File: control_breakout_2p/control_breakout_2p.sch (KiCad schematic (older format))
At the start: 8 parts, among them J1 DB15_Female_MountingHoles, J2 DB15_Female_MountingHoles, J3 Conn_02x12_Row_Letter_Last, J4 Conn_02x12_Row_Letter_Last, J5 Screw_Terminal_01x06, J6 Screw_Terminal_01x06

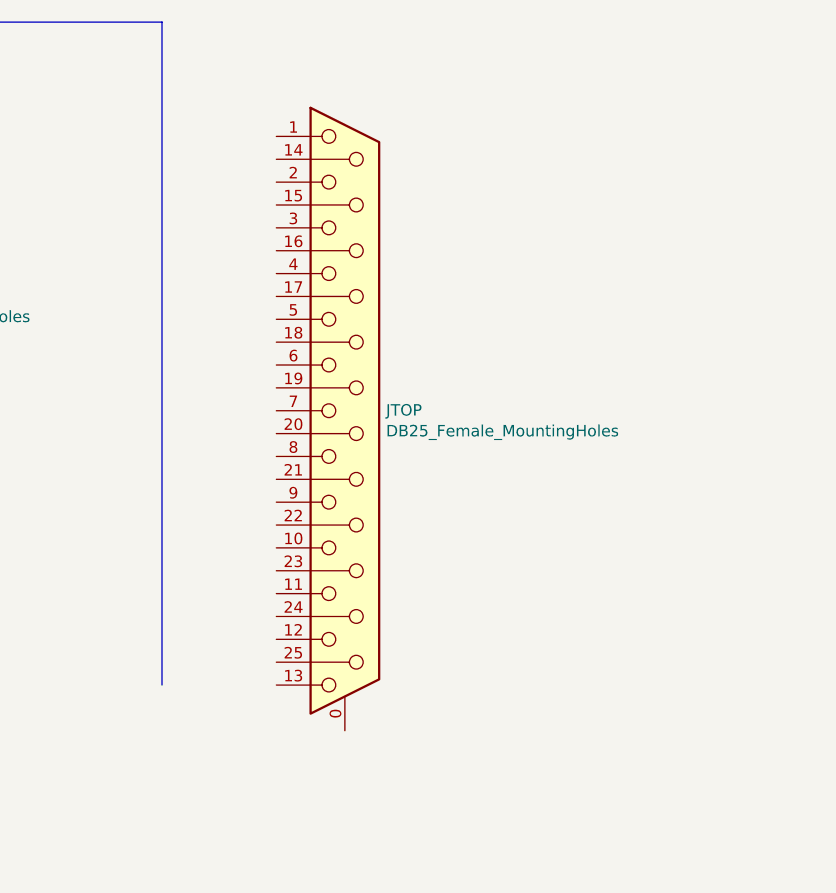
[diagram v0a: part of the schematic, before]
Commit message: Wire up proj pins
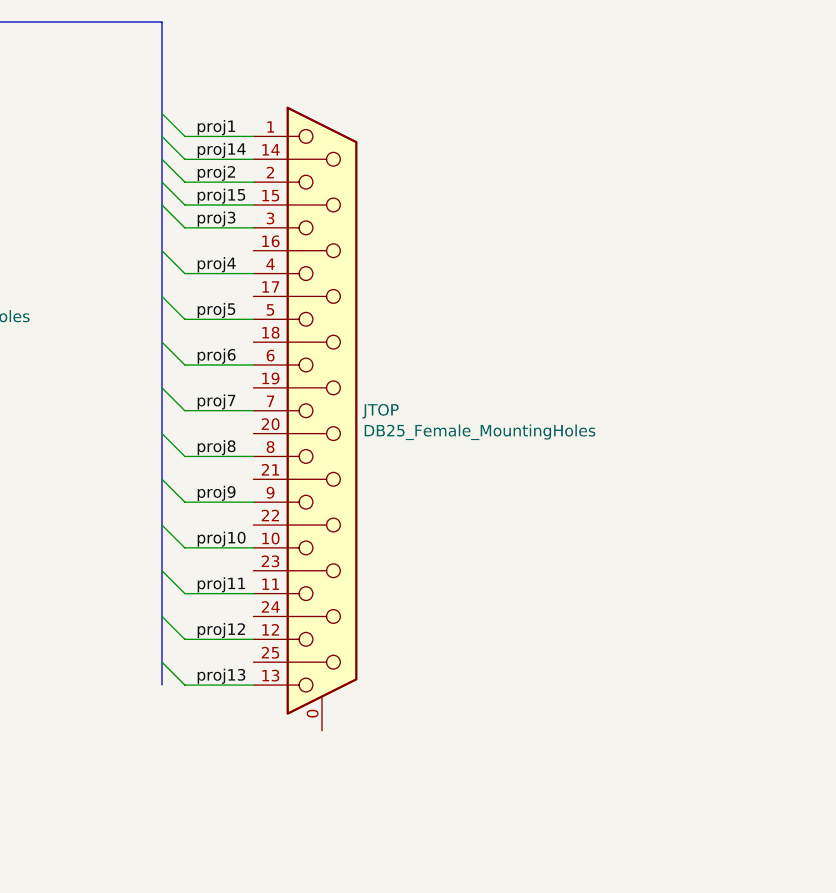
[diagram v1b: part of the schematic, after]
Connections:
- net proj1: now also JTOP.1
- net proj10: now also JTOP.10
- net proj11: now also JTOP.11
- net proj12: now also JTOP.12
- net proj13: now also JTOP.13
- net proj14: now also JTOP.14 (P14)
- net proj15: now also JTOP.15 (P15)
- net proj2: now also JTOP.2
- net proj3: now also JTOP.3
- net proj4: now also JTOP.4
- net proj5: now also JTOP.5
- net proj6: now also JTOP.6
- net proj7: now also JTOP.7
- net proj8: now also JTOP.8
- net proj9: now also JTOP.9
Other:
- moved on the sheet: JTOP
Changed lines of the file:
@@
 L Connector:DB25_Female_MountingHoles JTOP
 U 1 1 60C4D379
-P 6000 2500
-F 0 "JTOP" H 6180 2502 50  0000 L CNN
-F 1 "DB25_Female_MountingHoles" H 6180 2411 50  0000 L CNN
-F 2 "" H 6000 2500 50  0001 C CNN
-F 3 " ~" H 6000 2500 50  0001 C CNN
-	1    6000 2500
+P 5900 2500
+F 0 "JTOP" H 6080 2502 50  0000 L CNN
+F 1 "DB25_Female_MountingHoles" H 6080 2411 50  0000 L CNN
+F 2 "" H 5900 2500 50  0001 C CNN
+F 3 " ~" H 5900 2500 50  0001 C CNN
+	1    5900 2500
 	1    0    0    -1
 $EndComp
@@
 Wire Bus Line
 	2750 800  5200 800
-Wire Bus Line
-	5200 800  5200 3700
 Connection ~ 2750 800
 Entry Wire Line
@@
 Text Label 2900 2700 0    50   ~ 0
 proj8
+Entry Wire Line
+	5200 1200 5300 1300
+Entry Wire Line
+	5200 2800 5300 2900
+Entry Wire Line
+	5200 1400 5300 1500
+Entry Wire Line
+	5200 3000 5300 3100
+Entry Wire Line
+	5200 1600 5300 1700
+Entry Wire Line
+	5200 3200 5300 3300
+Entry Wire Line
+	5200 1800 5300 1900
+Entry Wire Line
+	5200 3400 5300 3500
+Entry Wire Line
+	5200 2000 5300 2100
+Entry Wire Line
+	5200 3600 5300 3700
+Entry Wire Line
+	5200 2200 5300 2300
+Entry Wire Line
+	5200 1300 5300 1400
+Entry Wire Line
+	5200 2400 5300 2500
+Entry Wire Line
+	5200 1500 5300 1600
+Entry Wire Line
+	5200 2600 5300 2700
+Wire Wire Line
+	5300 1300 5600 1300
+Wire Wire Line
+	5300 2900 5600 2900
+Wire Wire Line
+	5300 1500 5600 1500
+Wire Wire Line
+	5300 1700 5600 1700
+Wire Wire Line
+	5300 1900 5600 1900
+Wire Wire Line
+	5300 2100 5600 2100
+Wire Wire Line
+	5300 2300 5600 2300
+Wire Wire Line
+	5300 2500 5600 2500
+Wire Wire Line
+	5300 2700 5600 2700
+Text Label 5350 1300 0    50   ~ 0
+proj1
+Text Label 5350 2900 0    50   ~ 0
+proj9
+Text Label 5350 1500 0    50   ~ 0
+proj2
+Text Label 5350 3100 0    50   ~ 0
+proj10
+Text Label 5350 1700 0    50   ~ 0
+proj3
+Text Label 5350 3300 0    50   ~ 0
+proj11
+Text Label 5350 1900 0    50   ~ 0
+proj4
+Text Label 5350 3500 0    50   ~ 0
+proj12
+Text Label 5350 2100 0    50   ~ 0
+proj5
+Text Label 5350 3700 0    50   ~ 0
+proj13
+Text Label 5350 2300 0    50   ~ 0
+proj6
+Text Label 5350 1400 0    50   ~ 0
+proj14
+Text Label 5350 2500 0    50   ~ 0
+proj7
+Text Label 5350 1600 0    50   ~ 0
+proj15
+Text Label 5350 2700 0    50   ~ 0
+proj8
+Wire Wire Line
+	5300 1600 5600 1600
+Wire Wire Line
+	5300 1400 5600 1400
+Wire Wire Line
+	5300 3100 5600 3100
+Wire Wire Line
+	5300 3300 5600 3300
+Wire Wire Line
+	5300 3500 5600 3500
+Wire Wire Line
+	5300 3700 5600 3700
+Wire Bus Line
+	5200 800  5200 3700
 Wire Bus Line
 	2750 800  2750 2700
